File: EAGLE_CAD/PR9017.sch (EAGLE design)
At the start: 76 parts, among them SW1 C&K_PTS645, Y1 ABS25XTAL

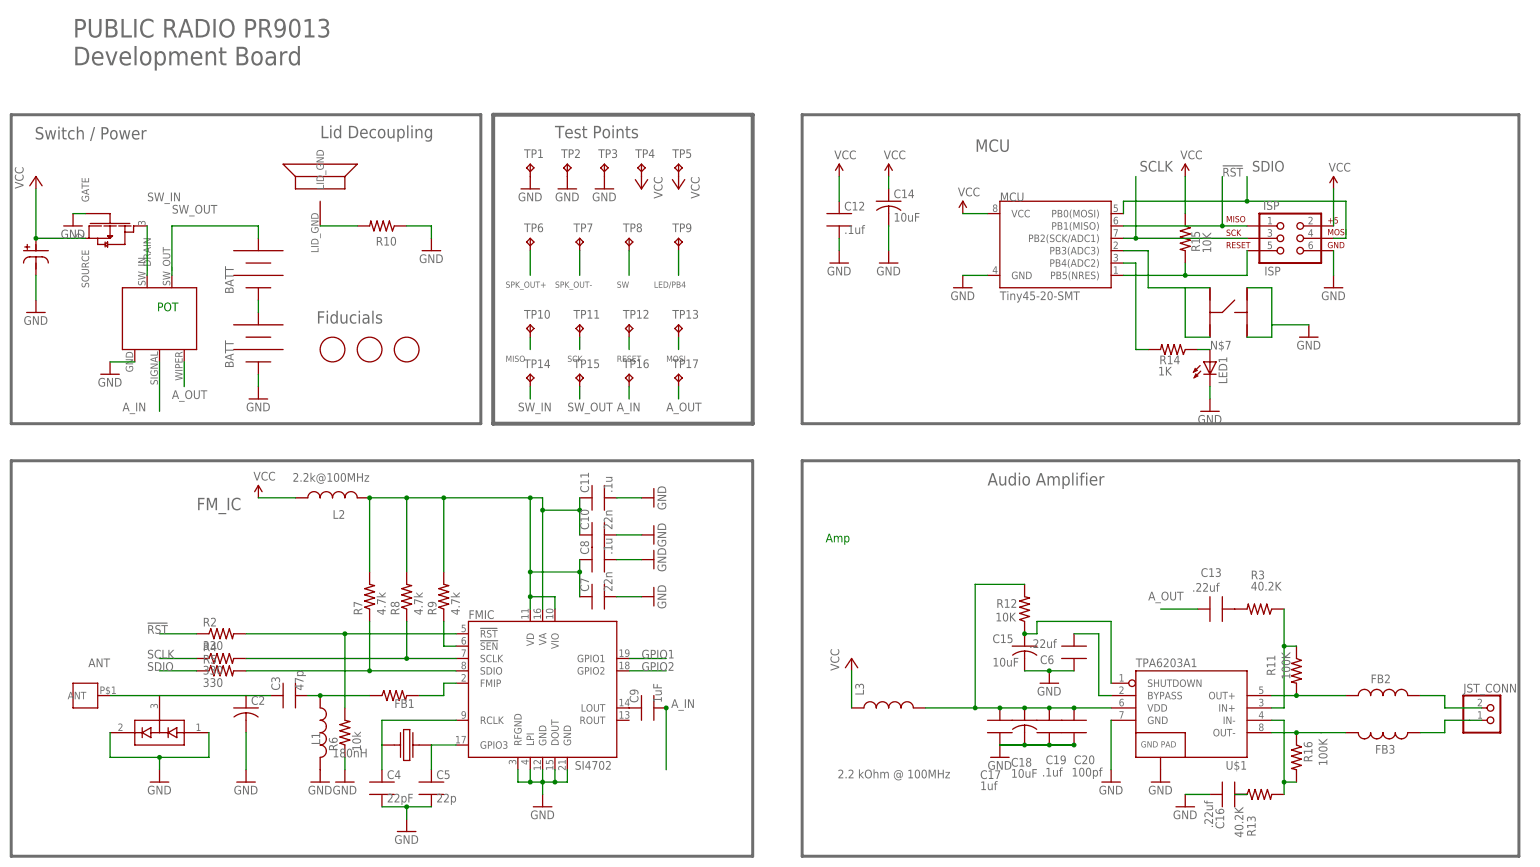
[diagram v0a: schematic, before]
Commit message: small amp changes
ripped up a few things.

the test pads on the speaker were at the wrong point (on the sch) so i
fixed that.

then rerouted most of the amp section. don’t love it, but it’s a start.
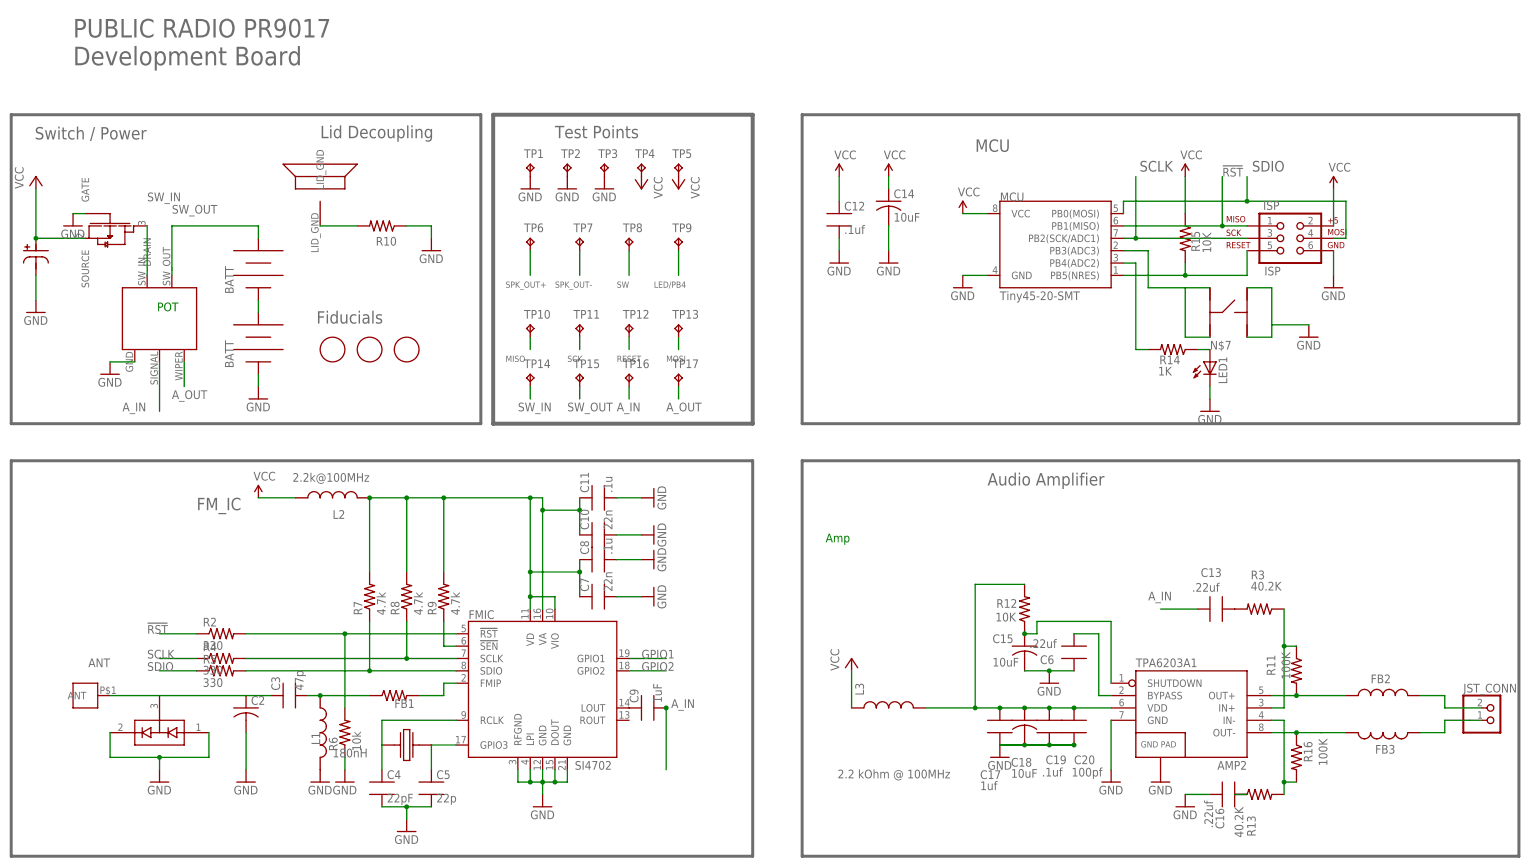
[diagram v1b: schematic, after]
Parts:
- renumbered U$1 to AMP2
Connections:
- removed net N$17: FB2.2, JST_CONN.1
- removed net N$4: FB3.1, JST_CONN.2
- net A_IN: now also C13.1
- net A_OUT: no longer C13.1
- net SPK_OUT+: now also FB2.2, JST_CONN.1
- net SPK_OUT-: now also FB3.1, JST_CONN.2
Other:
- note added: "PUBLIC RADIO PR9017 Development Board"
- note removed: "PUBLIC RADIO PR9013 Development Board"
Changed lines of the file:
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@@
 <?xml version="1.0" encoding="utf-8"?>
 <!DOCTYPE eagle SYSTEM "eagle.dtd">
-<eagle version="6.6.0">
+<eagle version="7.2.0">
 <drawing>
 <settings>
@@
 <part name="GND15" library="SparkFun-Aesthetics" deviceset="GND" device=""/>
 <part name="R3" library="PR_Parts_Library" deviceset="RES_SMT" device="" value="40.2K"/>
-<part name="U$1" library="PR_Parts_Library" deviceset="TPA6203A1" device=""/>
+<part name="AMP2" library="PR_Parts_Library" deviceset="TPA6203A1" device=""/>
 <part name="R11" library="PR_Parts_Library" deviceset="RES_SMT" device="" value="100K"/>
 <part name="R16" library="PR_Parts_Library" deviceset="RES_SMT" device="" value="100K"/>
@@
 <text x="160.02" y="76.2" size="2.54" layer="96">Audio Amplifier </text>
 <text x="157.48" y="144.78" size="2.54" layer="96">MCU</text>
-<text x="-27.94" y="162.56" size="3.81" layer="96">PUBLIC RADIO PR9013
+<text x="-27.94" y="162.56" size="3.81" layer="96">PUBLIC RADIO PR9017
 Development Board </text>
 <text x="22.098" y="109.474" size="2.54" layer="96">Fiducials </text>
@@
 <attribute name="VALUE" x="214.122" y="54.61" size="1.778" layer="96"/>
 </instance>
-<instance part="U$1" gate="G$1" x="200.66" y="30.48"/>
+<instance part="AMP2" gate="G$1" x="200.66" y="30.48"/>
 <instance part="R11" gate="G$1" x="223.52" y="38.1" smashed="yes" rot="R270">
 <attribute name="NAME" x="217.3986" y="41.402" size="1.778" layer="95" rot="R270"/>
@@
 </segment>
 <segment>
-<pinref part="U$1" gate="G$1" pin="GND@2"/>
+<pinref part="AMP2" gate="G$1" pin="GND@2"/>
 <pinref part="GND18" gate="1" pin="GND"/>
 </segment>
@@
 </segment>
 <segment>
-<pinref part="U$1" gate="G$1" pin="GND@1"/>
+<pinref part="AMP2" gate="G$1" pin="GND@1"/>
 <wire x1="185.42" y1="27.94" x2="185.42" y2="17.78" width="0.1524" layer="91"/>
 <pinref part="GND15" gate="1" pin="GND"/>
@@
 <pinref part="R12" gate="G$1" pin="1"/>
 <pinref part="C15" gate="G$1" pin="1"/>
-<pinref part="U$1" gate="G$1" pin="SHUTDOWN"/>
+<pinref part="AMP2" gate="G$1" pin="SHUTDOWN"/>
 <wire x1="185.42" y1="35.56" x2="185.42" y2="48.26" width="0.1524" layer="91"/>
 <wire x1="185.42" y1="48.26" x2="170.18" y2="48.26" width="0.1524" layer="91"/>
@@
 </segment>
 <segment>
-<pinref part="C13" gate="G$1" pin="1"/>
-<wire x1="203.2" y1="50.8" x2="195.58" y2="50.8" width="0.1524" layer="91"/>
-<label x="193.04" y="52.578" size="1.778" layer="95"/>
-</segment>
-<segment>
 <pinref part="TP17" gate="G$1" pin="TP"/>
 <wire x1="96.52" y1="96.52" x2="96.52" y2="93.98" width="0.1524" layer="91"/>
@@
 <wire x1="86.36" y1="96.52" x2="86.36" y2="93.98" width="0.1524" layer="91"/>
 <label x="83.82" y="91.44" size="1.778" layer="95"/>
+</segment>
+<segment>
+<pinref part="C13" gate="G$1" pin="1"/>
+<wire x1="203.2" y1="50.8" x2="195.58" y2="50.8" width="0.1524" layer="91"/>
+<label x="193.04" y="52.578" size="1.778" layer="95"/>
 </segment>
 </net>
@@
 <label x="60.96" y="116.84" size="1.27" layer="95"/>
 </segment>
+<segment>
+<pinref part="FB2" gate="G$1" pin="2"/>
+<wire x1="248.92" y1="33.02" x2="254" y2="33.02" width="0.1524" layer="91"/>
+<wire x1="254" y1="33.02" x2="254" y2="30.48" width="0.1524" layer="91"/>
+<pinref part="JST_CONN" gate="G$1" pin="1"/>
+<wire x1="254" y1="30.48" x2="261.62" y2="30.48" width="0.1524" layer="91"/>
+</segment>
 </net>
 <net name="SPK_OUT-" class="0">
@@
 <wire x1="76.2" y1="124.46" x2="76.2" y2="119.38" width="0.1524" layer="91"/>
 <label x="71.12" y="116.84" size="1.27" layer="95"/>
+</segment>
+<segment>
+<pinref part="FB3" gate="G$1" pin="1"/>
+<wire x1="248.92" y1="25.4" x2="254" y2="25.4" width="0.1524" layer="91"/>
+<wire x1="254" y1="25.4" x2="254" y2="27.94" width="0.1524" layer="91"/>
+<pinref part="JST_CONN" gate="G$1" pin="2"/>
+<wire x1="254" y1="27.94" x2="259.08" y2="27.94" width="0.1524" layer="91"/>
+<wire x1="261.62" y1="27.94" x2="259.08" y2="27.94" width="0.1524" layer="91"/>
 </segment>
 </net>
@@
 <net name="N$5" class="0">
 <segment>
-<pinref part="U$1" gate="G$1" pin="IN-"/>
+<pinref part="AMP2" gate="G$1" pin="IN-"/>
 <wire x1="218.44" y1="27.94" x2="220.98" y2="27.94" width="0.1524" layer="91"/>
 <pinref part="R13" gate="G$1" pin="2"/>
@@
 <net name="N$14" class="0">
 <segment>
-<pinref part="U$1" gate="G$1" pin="IN+"/>
+<pinref part="AMP2" gate="G$1" pin="IN+"/>
 <wire x1="218.44" y1="30.48" x2="220.98" y2="30.48" width="0.1524" layer="91"/>
 <pinref part="R3" gate="G$1" pin="1"/>
@@
 <pinref part="L3" gate="G$1" pin="2"/>
 <junction x="162.56" y="30.48"/>
-<pinref part="U$1" gate="G$1" pin="VDD"/>
+<pinref part="AMP2" gate="G$1" pin="VDD"/>
 <wire x1="177.8" y1="30.48" x2="185.42" y2="30.48" width="0.1524" layer="91"/>
 <junction x="177.8" y="30.48"/>
@@
 </segment>
 </net>
-<net name="N$4" class="0">
-<segment>
-<pinref part="FB3" gate="G$1" pin="1"/>
-<wire x1="248.92" y1="25.4" x2="254" y2="25.4" width="0.1524" layer="91"/>
-<wire x1="254" y1="25.4" x2="254" y2="27.94" width="0.1524" layer="91"/>
-<pinref part="JST_CONN" gate="G$1" pin="2"/>
-<wire x1="254" y1="27.94" x2="259.08" y2="27.94" width="0.1524" layer="91"/>
-<wire x1="261.62" y1="27.94" x2="259.08" y2="27.94" width="0.1524" layer="91"/>
-</segment>
-</net>
-<net name="N$17" class="0">
-<segment>
-<pinref part="FB2" gate="G$1" pin="2"/>
-<wire x1="248.92" y1="33.02" x2="254" y2="33.02" width="0.1524" layer="91"/>
-<wire x1="254" y1="33.02" x2="254" y2="30.48" width="0.1524" layer="91"/>
-<pinref part="JST_CONN" gate="G$1" pin="1"/>
-<wire x1="254" y1="30.48" x2="261.62" y2="30.48" width="0.1524" layer="91"/>
-</segment>
-</net>
 <net name="N$12" class="0">
 <segment>
-<pinref part="U$1" gate="G$1" pin="BYPASS"/>
+<pinref part="AMP2" gate="G$1" pin="BYPASS"/>
 <wire x1="185.42" y1="33.02" x2="182.88" y2="33.02" width="0.1524" layer="91"/>
 <wire x1="182.88" y1="33.02" x2="182.88" y2="45.72" width="0.1524" layer="91"/>
@@
 <net name="N$11" class="0">
 <segment>
-<pinref part="U$1" gate="G$1" pin="OUT+"/>
+<pinref part="AMP2" gate="G$1" pin="OUT+"/>
 <pinref part="R11" gate="G$1" pin="2"/>
 <wire x1="223.52" y1="33.02" x2="218.44" y2="33.02" width="0.1524" layer="91"/>
@@
 <net name="N$15" class="0">
 <segment>
-<pinref part="U$1" gate="G$1" pin="OUT-"/>
+<pinref part="AMP2" gate="G$1" pin="OUT-"/>
 <pinref part="R16" gate="G$1" pin="1"/>
 <wire x1="223.52" y1="25.4" x2="218.44" y2="25.4" width="0.1524" layer="91"/>

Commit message: Updated Amp
Updated Amp SCH
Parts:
- removed C20: 100pf, PR_Parts_Library:CAP_SMT
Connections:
- net GND: no longer C20.2
- net N$14: now also AMP2.IN-; no longer AMP2.IN+
- net N$2: no longer C20.1
- net N$5: now also AMP2.IN+; no longer AMP2.IN-
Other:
- moved on the sheet: C16, C17, C18, C19, FB3, JST_CONN, L3, R16

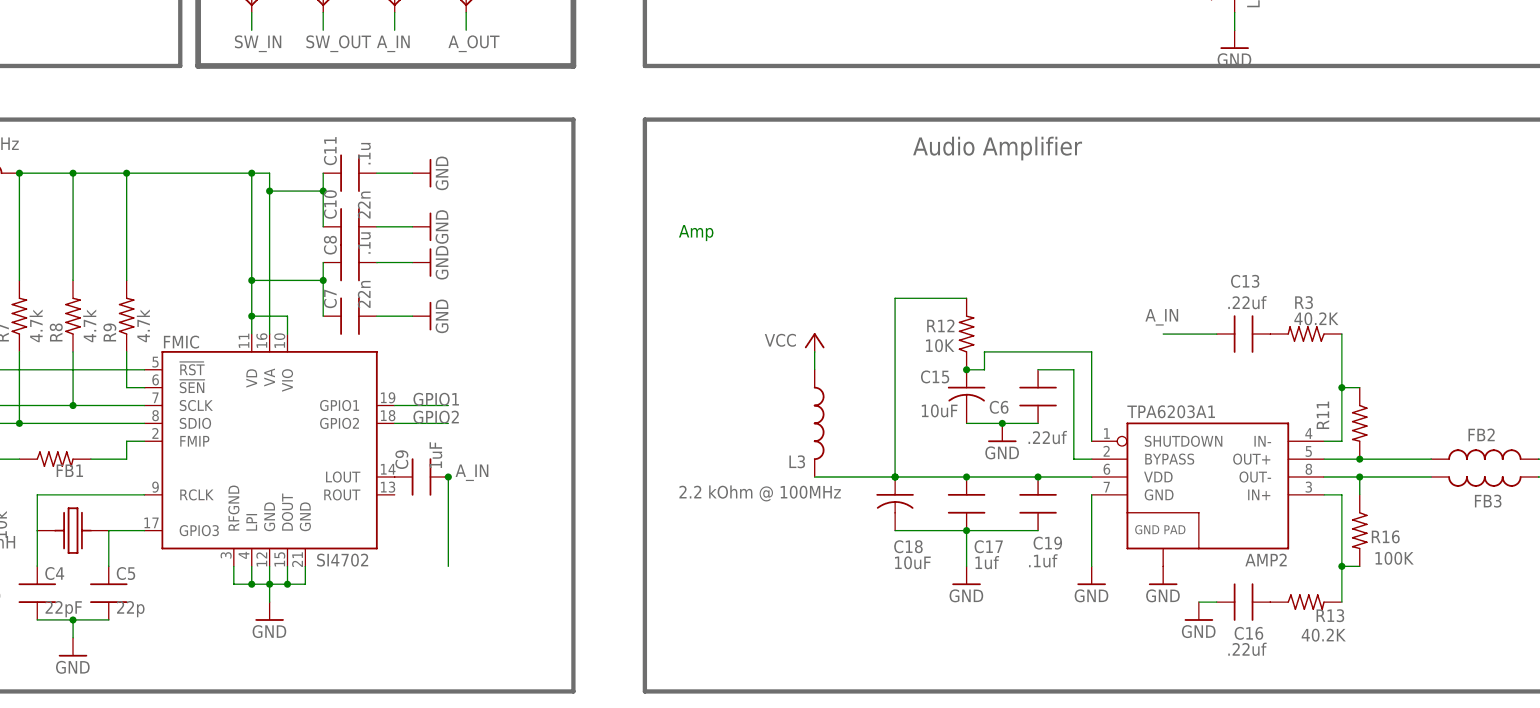
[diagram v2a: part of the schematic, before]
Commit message: Updated SCH
Updated the audio amp schematic with appropriate values for gain
setting resistors and input capacitors.
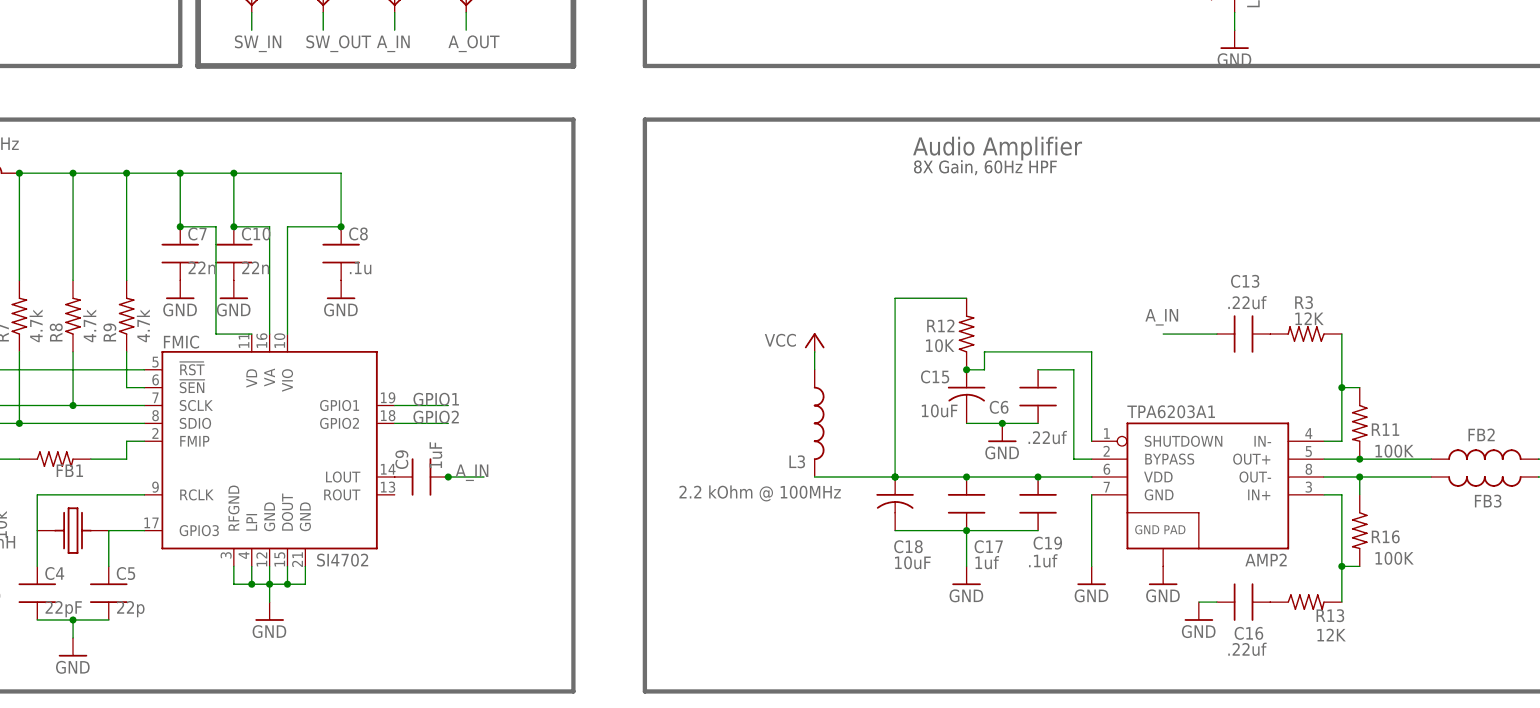
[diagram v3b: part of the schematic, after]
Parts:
- removed C11: .1u, PR_Parts_Library:CAP_SMT
- R13, R3: value 40.2K -> 12K
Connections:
- net 3.3V: no longer C11.1
- net GND: no longer C11.2
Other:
- note added: "8X Gain, 60Hz HPF"
- note removed: "Amp"
- moved on the sheet: C10, C7, C8
